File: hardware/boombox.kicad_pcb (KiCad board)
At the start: 2 copper layers, 13 parts, among them J1 Micro_SD_Card_Det1, J5 AudioJack4, U7 MCP7940MT-I/SN, U9 MCP73811T-420I-OT

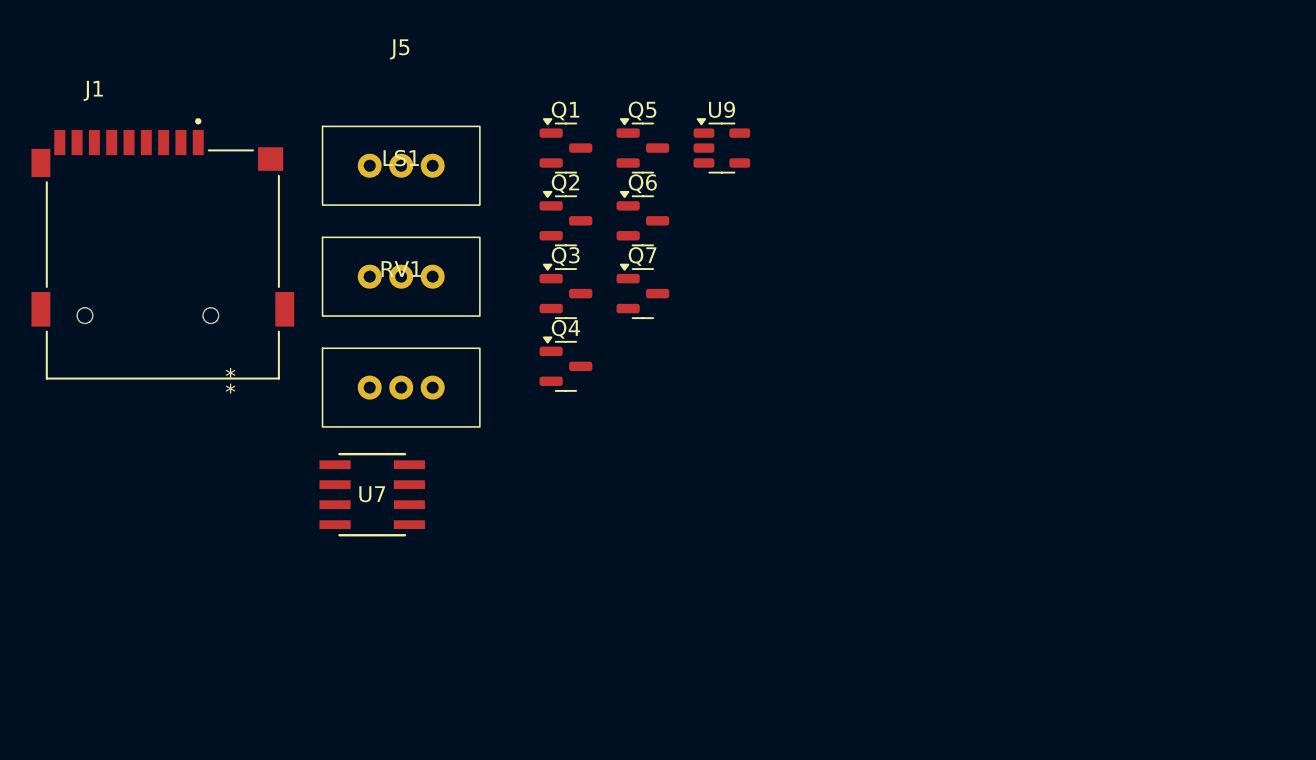
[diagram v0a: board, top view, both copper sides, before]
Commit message: Schematic done
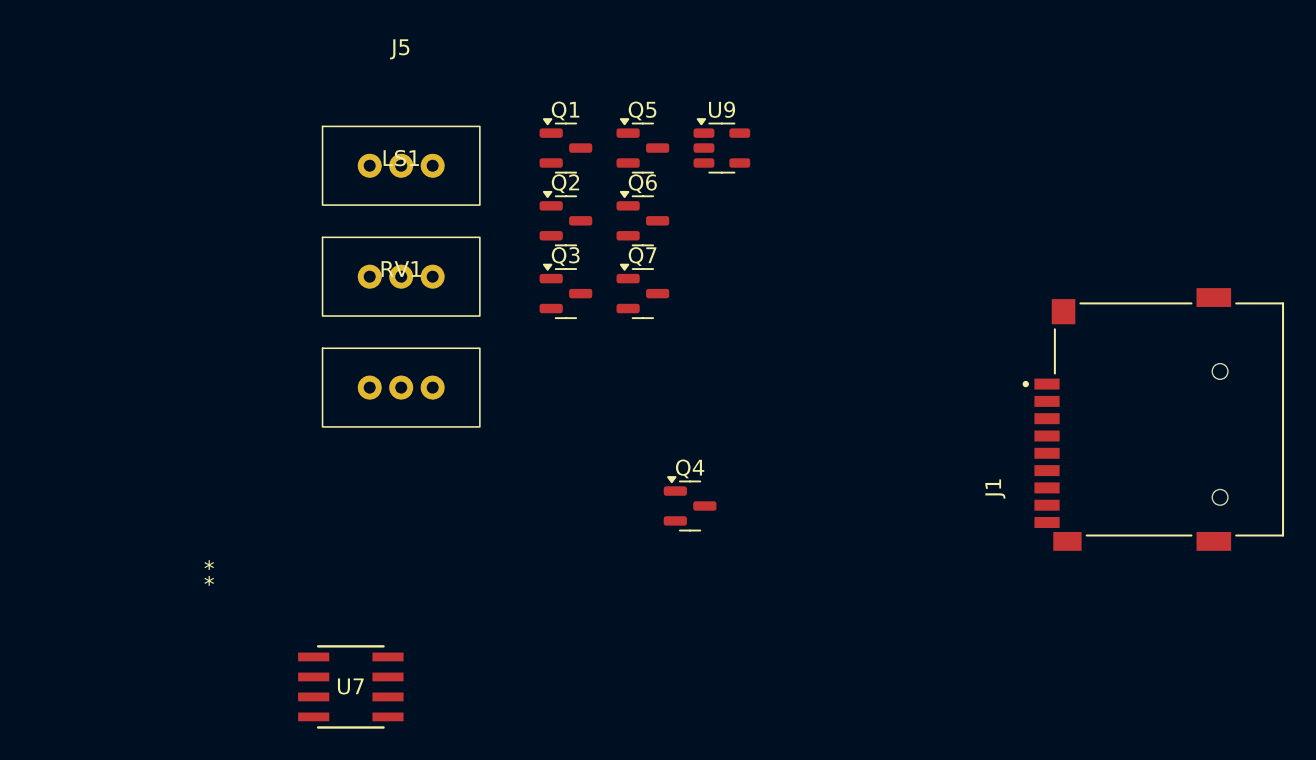
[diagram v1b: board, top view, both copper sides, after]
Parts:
- moved J1 64.7 mm to (192.5, 97.5), turned to 90 degrees
- moved U7 12.3 mm to (140.5, 114.5)
- moved Q4 11.9 mm to (162.1, 103.0)
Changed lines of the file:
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@@
 	(footprint "boombox:SOIC8-N_MC_MCH"
 		(layer "F.Cu")
-		(at 141.8605 102.2813)
+		(at 140.5 114.5)
 		(tags "MCP7940MT-I/SN ")
 		(property "Reference" "U7"
@@
 	(footprint "boombox:CUI_MSD-4-A"
 		(layer "F.Cu")
-		(at 128.5525 87.65)
+		(at 192.5 97.5 90)
 		(property "Reference" "J1"
-			(at -4.325 -11.135 0)
+			(at -4.325 -11.135 90)
 			(layer "F.SilkS")
 			(effects
@@
 		)
 		(property "Value" "Micro_SD_Card_Det1"
-			(at -0.515 -9.635 0)
+			(at -0.515 -9.635 90)
 			(layer "F.Fab")
 			(effects
@@
 		)
 		(property "Footprint" "boombox:CUI_MSD-4-A"
-			(at 0 0 0)
+			(at 0 0 90)
 			(layer "F.Fab")
 			(hide yes)
@@
 		)
 		(property "Datasheet" "${KIPRJMOD}/datasheets/MSD-4-A.pdf"
-			(at 0 0 0)
+			(at 0 0 90)
 			(layer "F.Fab")
 			(hide yes)
@@
 		)
 		(property "Description" "Micro SD Card Socket with one card detection pin"
-			(at 0 0 0)
+			(at 0 0 90)
 			(layer "F.Fab")
 			(hide yes)
@@
 		(attr smd)
 		(fp_line
+			(start 5.73 -7.25)
+			(end 2.92 -7.25)
+			(stroke
+				(width 0.127)
+				(type solid)
+			)
+			(layer "F.SilkS")
+		)
+		(fp_line
+			(start 7.375 -5.63)
+			(end 7.375 1.43)
+			(stroke
+				(width 0.127)
+				(type solid)
+			)
+			(layer "F.SilkS")
+		)
+		(fp_line
 			(start -7.375 -5.23)
 			(end -7.375 1.43)
@@
 		)
 		(fp_line
+			(start 7.375 4.27)
+			(end 7.375 7.25)
+			(stroke
+				(width 0.127)
+				(type solid)
+			)
+			(layer "F.SilkS")
+		)
+		(fp_line
 			(start -7.375 4.27)
 			(end -7.375 7.25)
@@
 		(fp_line
 			(start -7.375 7.25)
-			(end 7.375 7.25)
-			(stroke
-				(width 0.127)
-				(type solid)
-			)
-			(layer "F.SilkS")
-		)
-		(fp_line
-			(start 5.73 -7.25)
-			(end 2.92 -7.25)
-			(stroke
-				(width 0.127)
-				(type solid)
-			)
-			(layer "F.SilkS")
-		)
-		(fp_line
-			(start 7.375 -5.63)
-			(end 7.375 1.43)
-			(stroke
-				(width 0.127)
-				(type solid)
-			)
-			(layer "F.SilkS")
-		)
-		(fp_line
-			(start 7.375 4.27)
 			(end 7.375 7.25)
 			(stroke
@@
 		)
 		(fp_line
+			(start 8.6 -8.8)
+			(end 8.6 13.1)
+			(stroke
+				(width 0.05)
+				(type solid)
+			)
+			(layer "F.CrtYd")
+		)
+		(fp_line
 			(start -8.6 -8.8)
 			(end 8.6 -8.8)
@@
 		)
 		(fp_line
+			(start 8.6 13.1)
+			(end -8.6 13.1)
+			(stroke
+				(width 0.05)
+				(type solid)
+			)
+			(layer "F.CrtYd")
+		)
+		(fp_line
 			(start -8.6 13.1)
 			(end -8.6 -8.8)
@@
 		)
 		(fp_line
-			(start 8.6 -8.8)
-			(end 8.6 13.1)
-			(stroke
-				(width 0.05)
-				(type solid)
-			)
-			(layer "F.CrtYd")
-		)
-		(fp_line
-			(start 8.6 13.1)
-			(end -8.6 13.1)
-			(stroke
-				(width 0.05)
-				(type solid)
-			)
-			(layer "F.CrtYd")
+			(start 7.375 -7.25)
+			(end -7.375 -7.25)
+			(stroke
+				(width 0.127)
+				(type solid)
+			)
+			(layer "F.Fab")
 		)
 		(fp_line
@@
 		)
 		(fp_line
+			(start 7.375 7.25)
+			(end 7.375 -7.25)
+			(stroke
+				(width 0.127)
+				(type solid)
+			)
+			(layer "F.Fab")
+		)
+		(fp_line
+			(start 4.55 7.25)
+			(end 7.375 7.25)
+			(stroke
+				(width 0.127)
+				(type solid)
+			)
+			(layer "F.Fab")
+		)
+		(fp_line
+			(start -6.45 7.25)
+			(end 4.55 7.25)
+			(stroke
+				(width 0.127)
+				(type solid)
+			)
+			(layer "F.Fab")
+		)
+		(fp_line
+			(start -6.45 7.25)
+			(end -6.45 12.35)
+			(stroke
+				(width 0.127)
+				(type solid)
+			)
+			(layer "F.Fab")
+		)
+		(fp_line
 			(start -7.375 7.25)
 			(end -6.45 7.25)
@@
 		)
 		(fp_line
-			(start -6.45 7.25)
-			(end -6.45 12.35)
-			(stroke
-				(width 0.127)
-				(type solid)
-			)
-			(layer "F.Fab")
-		)
-		(fp_line
-			(start -6.45 7.25)
-			(end 4.55 7.25)
-			(stroke
-				(width 0.127)
-				(type solid)
-			)
-			(layer "F.Fab")
-		)
-		(fp_line
 			(start -5.95 9.55)
 			(end 4.05 9.55)
@@
 		)
 		(fp_line
+			(start 4.55 12.35)
+			(end 4.55 7.25)
+			(stroke
+				(width 0.127)
+				(type solid)
+			)
+			(layer "F.Fab")
+		)
+		(fp_line
 			(start -5.95 12.85)
 			(end 4.05 12.85)
@@
 			(layer "F.Fab")
 		)
-		(fp_line
-			(start 4.55 7.25)
-			(end 7.375 7.25)
-			(stroke
-				(width 0.127)
-				(type solid)
-			)
-			(layer "F.Fab")
-		)
-		(fp_line
-			(start 4.55 12.35)
-			(end 4.55 7.25)
-			(stroke
-				(width 0.127)
-				(type solid)
-			)
-			(layer "F.Fab")
-		)
-		(fp_line
-			(start 7.375 -7.25)
-			(end -7.375 -7.25)
-			(stroke
-				(width 0.127)
-				(type solid)
-			)
-			(layer "F.Fab")
-		)
-		(fp_line
-			(start 7.375 7.25)
-			(end 7.375 -7.25)
+		(fp_arc
+			(start 4.55 9.05)
+			(mid 4.403553 9.403553)
+			(end 4.05 9.55)
 			(stroke
 				(width 0.127)
@@
 		)
 		(fp_arc
+			(start 4.55 12.35)
+			(mid 4.403553 12.703553)
+			(end 4.05 12.85)
+			(stroke
+				(width 0.127)
+				(type solid)
+			)
+			(layer "F.Fab")
+		)
+		(fp_arc
 			(start -5.95 12.85)
 			(mid -6.303553 12.703553)
@@
 			(layer "F.Fab")
 		)
-		(fp_arc
-			(start 4.55 9.05)
-			(mid 4.403553 9.403553)
-			(end 4.05 9.55)
-			(stroke
-				(width 0.127)
-				(type solid)
-			)
-			(layer "F.Fab")
-		)
-		(fp_arc
-			(start 4.55 12.35)
-			(mid 4.403553 12.703553)
-			(end 4.05 12.85)
-			(stroke
-				(width 0.127)
-				(type solid)
-			)
-			(layer "F.Fab")
-		)
 		(fp_circle
 			(center 2.25 -9.1)
@@
 		)
 		(pad "" np_thru_hole circle
-			(at -4.95 3.25)
+			(at -4.95 3.25 90)
 			(size 1 1)
 			(drill 1)
@@
 		)
 		(pad "" np_thru_hole circle
-			(at 3.05 3.25)
+			(at 3.05 3.25 90)
 			(size 1 1)
 			(drill 1)
@@
 		)
 		(pad "1" smd rect
-			(at 2.25 -7.75)
+			(at 2.25 -7.75 90)
 			(size 0.7 1.6)
 			(layers "F.Cu" "F.Paste" "F.Mask")
@@
 		)
 		(pad "2" smd rect
-			(at 1.15 -7.75)
+			(at 1.15 -7.75 90)
 			(size 0.7 1.6)
 			(layers "F.Cu" "F.Paste" "F.Mask")
@@
 		)
 		(pad "3" smd rect
-			(at 0.05 -7.75)
+			(at 0.05 -7.75 90)
 			(size 0.7 1.6)
 			(layers "F.Cu" "F.Paste" "F.Mask")
@@
 		)
 		(pad "4" smd rect
-			(at -1.05 -7.75)
+			(at -1.05 -7.75 90)
 			(size 0.7 1.6)
 			(layers "F.Cu" "F.Paste" "F.Mask")
@@
 		)
 		(pad "5" smd rect
-			(at -2.15 -7.75)
+			(at -2.15 -7.75 90)
 			(size 0.7 1.6)
 			(layers "F.Cu" "F.Paste" "F.Mask")
@@
 		)
 		(pad "6" smd rect
-			(at -3.25 -7.75)
+			(at -3.25 -7.75 90)
 			(size 0.7 1.6)
 			(layers "F.Cu" "F.Paste" "F.Mask")
@@
 		)
 		(pad "7" smd rect
-			(at -4.35 -7.75)
+			(at -4.35 -7.75 90)
 			(size 0.7 1.6)
 			(layers "F.Cu" "F.Paste" "F.Mask")
@@
 		)
 		(pad "8" smd rect
-			(at -5.45 -7.75)
+			(at -5.45 -7.75 90)
 			(size 0.7 1.6)
 			(layers "F.Cu" "F.Paste" "F.Mask")
@@
 		)
 		(pad "CD" smd rect
-			(at -6.55 -7.75)
+			(at -6.55 -7.75 90)
 			(size 0.7 1.6)
 			(layers "F.Cu" "F.Paste" "F.Mask")
@@
 		)
 		(pad "G1" smd rect
-			(at -7.75 -6.45)
+			(at -7.75 -6.45 90)
 			(size 1.2 1.8)
 			(layers "F.Cu" "F.Paste" "F.Mask")
@@
 		)
 		(pad "G2" smd rect
-			(at 6.85 -6.7)
+			(at 6.85 -6.7 90)
 			(size 1.6 1.5)
 			(layers "F.Cu" "F.Paste" "F.Mask")
@@
 		)
 		(pad "G3" smd rect
-			(at -7.75 2.85)
+			(at -7.75 2.85 90)
 			(size 1.2 2.2)
 			(layers "F.Cu" "F.Paste" "F.Mask")
@@
 		)
 		(pad "G4" smd rect
-			(at 7.75 2.85)
+			(at 7.75 2.85 90)
 			(size 1.2 2.2)
 			(layers "F.Cu" "F.Paste" "F.Mask")
@@
 	(footprint "Package_TO_SOT_SMD:SOT-23"
 		(layer "F.Cu")
-		(at 154.1725 94.125)
+		(at 162.0625 103)
 		(descr "SOT, 3 Pin (https://www.jedec.org/system/files/docs/to-236h.pdf variant AB), generated with kicad-footprint-generator ipc_gullwing_generator.py")
 		(tags "SOT TO_SOT_SMD")

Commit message: Comitting so Nate can see errors
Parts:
- removed J1: Micro_SD_Card_Det1, boombox:CUI_MSD-4-A
- removed J5: AudioJack4, boombox:Degson 3 Pin
- removed LS1: Speaker, boombox:Degson 3 Pin
- removed Q1, Q2, Q3, Q4, Q5, Q6, Q7: ~, Package_TO_SOT_SMD:SOT-23
- removed RV1: R_Potentiometer_US, boombox:Degson 3 Pin
- removed U7: MCP7940MT-I/SN, boombox:SOIC8-N_MC_MCH
- removed U9: MCP73811T-420I-OT, Package_TO_SOT_SMD:SOT-23-5
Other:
- board outline added: 85 x 70 mm

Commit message: Routing
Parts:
- added C1: 6pF, Capacitor_SMD:C_0402_1005Metric_Pad0.74x0.62mm_HandSolder, F.Cu at (129.4, 89.5)
- added C10: 0.1uF, Capacitor_SMD:C_0402_1005Metric_Pad0.74x0.62mm_HandSolder, F.Cu at (85.5, 121.7)
- added C11: 0.1uF, Capacitor_SMD:C_0402_1005Metric_Pad0.74x0.62mm_HandSolder, F.Cu at (85.5, 123.7)
- added C12: 0.1uF, Capacitor_SMD:C_0402_1005Metric_Pad0.74x0.62mm_HandSolder, F.Cu at (85.5, 125.7)
- added C13: 0.1uF, Capacitor_SMD:C_0402_1005Metric_Pad0.74x0.62mm_HandSolder, F.Cu at (88.7, 117.8)
- added C14: 0.1uF, Capacitor_SMD:C_0402_1005Metric_Pad0.74x0.62mm_HandSolder, F.Cu at (88.7, 119.8)
- added C15: 0.1uF, Capacitor_SMD:C_0402_1005Metric_Pad0.74x0.62mm_HandSolder, F.Cu at (88.7, 121.7)
- added C16: 0.1uF, Capacitor_SMD:C_0402_1005Metric_Pad0.74x0.62mm_HandSolder, F.Cu at (88.7, 123.7)
- added C17: 0.1uF, Capacitor_SMD:C_0402_1005Metric_Pad0.74x0.62mm_HandSolder, F.Cu at (73.1, 120.8)
- added C18: 0.1uF, Capacitor_SMD:C_0402_1005Metric_Pad0.74x0.62mm_HandSolder, F.Cu at (132.6, 165.5)
- added C19: 0.1uF, Capacitor_SMD:C_0402_1005Metric_Pad0.74x0.62mm_HandSolder, F.Cu at (132.6, 167.5)
- added C2: 1nF, Capacitor_SMD:C_0402_1005Metric_Pad0.74x0.62mm_HandSolder, F.Cu at (119.2, 87.2)
- added C20: 0.1uF, Capacitor_SMD:C_0402_1005Metric_Pad0.74x0.62mm_HandSolder, F.Cu at (132.6, 169.4)
- added C21: 10uF, Capacitor_SMD:C_0603_1608Metric_Pad1.08x0.95mm_HandSolder, F.Cu at (193.2, 131.3)
- added C22: 10uF, Capacitor_SMD:C_0603_1608Metric_Pad1.08x0.95mm_HandSolder, F.Cu at (133.1, 171.7)
- added C23: 10uF, Capacitor_SMD:C_0603_1608Metric_Pad1.08x0.95mm_HandSolder, F.Cu at (133.1, 174.2)
- added C3: 6pF, Capacitor_SMD:C_0402_1005Metric_Pad0.74x0.62mm_HandSolder, F.Cu at (128.5, 71.7)
- added C4: 6pF, Capacitor_SMD:C_0402_1005Metric_Pad0.74x0.62mm_HandSolder, F.Cu at (126.6, 78.2)
- added C5: 1nF, Capacitor_SMD:C_0402_1005Metric_Pad0.74x0.62mm_HandSolder, F.Cu at (132.8, 60.2)
- added C6: 1nF, Capacitor_SMD:C_0402_1005Metric_Pad0.74x0.62mm_HandSolder, F.Cu at (132.8, 62.1)
- added C7: 1nF, Capacitor_SMD:C_0402_1005Metric_Pad0.74x0.62mm_HandSolder, F.Cu at (132.8, 64.1)
- added C8: 1nF, Capacitor_SMD:C_0402_1005Metric_Pad0.74x0.62mm_HandSolder, F.Cu at (135.8, 61.4)
- added C9: 1nF, Capacitor_SMD:C_0402_1005Metric_Pad0.74x0.62mm_HandSolder, F.Cu at (135.8, 63.4)
- added D1: D_Dual_CommonCathode_AAK_Split, Package_TO_SOT_SMD:SOT-23, B.Cu at (135.8, 127.8)
- added D11: D_Schottky, Diode_SMD:D_SOD-123, F.Cu at (187.8, 130.1)
- added D12: D_Schottky, Diode_SMD:D_SOD-123, F.Cu at (188.4, 82.0)
- added D2: D_Dual_CommonCathode_AAK_Split, Package_TO_SOT_SMD:SOT-23, B.Cu at (135.7, 79.7)
- added D3: D_Dual_CommonCathode_AAK_Split, Package_TO_SOT_SMD:SOT-23, B.Cu at (136.6, 101.8)
- added D6: D_Dual_CommonCathode_AAK_Split, Package_TO_SOT_SMD:SOT-23, F.Cu at (108.0, -71.2)
- added D7: D_Dual_CommonCathode_AAK_Split, Package_TO_SOT_SMD:SOT-23, F.Cu at (108.0, -67.0)
- added D8: D_Dual_CommonCathode_AAK_Split, Package_TO_SOT_SMD:SOT-23, F.Cu at (108.0, -62.6)
- added J1: Micro_SD_Card_Det1, boombox:CUI_MSD-4-A, B.Cu at (113.7, 101.5)
- added J2: AudioJack4, boombox:EBAA02C_Audio, B.Cu at (185.3, 73.1)
- added J3: Battery, boombox:EBAA02C, B.Cu at (195.3, 73.1)
- added J4: USB_C_Receptacle_USB2.0_16P, boombox:CUI_UJ20-C-H-C-4-SMT-TR, F.Cu at (201.1, 126.5)
- added LS1: Speaker, boombox:EBAA02C, B.Cu at (175.3, 73.1)
- added Q1: ~, Package_TO_SOT_SMD:SOT-23, F.Cu at (116.6, 87.8)
- added Q2: ~, Package_TO_SOT_SMD:SOT-23, F.Cu at (112.5, 87.8)
- added Q3: ~, Package_TO_SOT_SMD:SOT-23, F.Cu at (181.9, 83.0)
- added Q4: ~, Package_TO_SOT_SMD:SOT-23, F.Cu at (132.7, 88.0)
- added Q5: ~, Package_TO_SOT_SMD:SOT-23, F.Cu at (95.7, -71.0)
- added Q6: ~, Package_TO_SOT_SMD:SOT-23, F.Cu at (132.7, 91.8)
- added Q7: ~, Package_TO_SOT_SMD:SOT-23, F.Cu at (114.7, 81.6)
- added R1: 3.3M, Resistor_SMD:R_0402_1005Metric_Pad0.72x0.64mm_HandSolder, F.Cu at (129.3, 90.9)
- added R10: 5.1k, Resistor_SMD:R_0402_1005Metric_Pad0.72x0.64mm_HandSolder, F.Cu at (193.7, 127.8)
- added R11: 5.1k, Resistor_SMD:R_0402_1005Metric_Pad0.72x0.64mm_HandSolder, F.Cu at (198.6, 119.5)
- added R12: 100k, Resistor_SMD:R_0402_1005Metric_Pad0.72x0.64mm_HandSolder, F.Cu at (126.0, 167.4)
- added R13: 0, Resistor_SMD:R_0402_1005Metric_Pad0.72x0.64mm_HandSolder, F.Cu at (126.0, 169.4)
- added R14: 0, Resistor_SMD:R_0402_1005Metric_Pad0.72x0.64mm_HandSolder, F.Cu at (126.0, 171.4)
- added R15: 0, Resistor_SMD:R_0402_1005Metric_Pad0.72x0.64mm_HandSolder, F.Cu at (126.6, 173.2)
- added R16: 1M, Resistor_SMD:R_0402_1005Metric_Pad0.72x0.64mm_HandSolder, F.Cu at (112.4, 172.9)
- added R2: 3.3M, Resistor_SMD:R_0402_1005Metric_Pad0.72x0.64mm_HandSolder, F.Cu at (129.3, 92.8)
- added R3: 1M, Resistor_SMD:R_0402_1005Metric_Pad0.72x0.64mm_HandSolder, F.Cu at (114.0, 85.4)
- added R4: 1M, Resistor_SMD:R_0402_1005Metric_Pad0.72x0.64mm_HandSolder, F.Cu at (109.5, 87.4)
- added R5: 100k, Resistor_SMD:R_0402_1005Metric_Pad0.72x0.64mm_HandSolder, F.Cu at (126.0, 165.4)
- added R6: 10k, Resistor_SMD:R_0402_1005Metric_Pad0.72x0.64mm_HandSolder, F.Cu at (137.4, 78.8)
- added R7: 10k, Resistor_SMD:R_0402_1005Metric_Pad0.72x0.64mm_HandSolder, F.Cu at (137.4, 77.5)
- added R8: 10k, Resistor_SMD:R_0402_1005Metric_Pad0.72x0.64mm_HandSolder, F.Cu at (194.3, 91.3)
- added R9: 10k, Resistor_SMD:R_0402_1005Metric_Pad0.72x0.64mm_HandSolder, F.Cu at (194.3, 94.0)
- added RV1: 500k, boombox:Degson 3 Pin, B.Cu at (174.2, 130.6)
- added SW1: SW_SPST, TestPoint:TestPoint_Pad_2.0x2.0mm, F.Cu at (72.8, -54.4)
- added SW2: SW_SPST, boombox:PTS645S_SMTR92_CNK, F.Cu at (96.7, -79.0)
- added SW3: SW_SPST, boombox:PTS645S_SMTR92_CNK, F.Cu at (107.5, -79.2)
- added SW4: SW_SPST, boombox:PTS645S_SMTR92_CNK, F.Cu at (128.5, -79.2)
- added SW5: SW_SPST, boombox:PTS645S_SMTR92_CNK, F.Cu at (118.0, -79.2)
- added U1: Pico, boombox:RPi_Pico_SMD_TH, F.Cu at (167.2, 102.3)
- added U10: MAX98365A, boombox:MAX98365, F.Cu at (164.0, 144.6)
- added U2: TMAG5231, Package_TO_SOT_SMD:SOT-23, B.Cu at (136.4, 98.0)
- added U3: TMAG5231, Package_TO_SOT_SMD:SOT-23, B.Cu at (151.4, 77.8)
- added U4: TMAG5231, Package_TO_SOT_SMD:SOT-23, B.Cu at (121.4, 77.8)
- added U5: TMAG5231, Package_TO_SOT_SMD:SOT-23, B.Cu at (121.4, 127.8)
- added U6: TMAG5231, Package_TO_SOT_SMD:SOT-23, B.Cu at (151.4, 127.8)
- added U7: MCP7940MT-I/SN, boombox:SOIC8-N_MC_MCH, F.Cu at (131.5, 76.9)
- added U8: MAX98365A, boombox:MAX98365, F.Cu at (115.0, 172.9)
- added U9: MCP73811T-420I-OT, Package_TO_SOT_SMD:SOT-23-5, F.Cu at (198.5, 83.0)
- added Y1: Crystal, boombox:XTAL_ECS-.327-6-13X, F.Cu at (124.7, 73.2)
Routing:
- net SLP_PWR: track 0.00 -> 204.5 mm, vias 0 -> 10
- net Net-(D1A-K): track 0.00 -> 73.1 mm, vias 0 -> 3
- net /Power/POWER IN: track 0.00 -> 70.3 mm, vias 0 -> 4
- net /Power/~{POWER_OFF}: track 0.00 -> 67.2 mm
- net Net-(J1-VDD): track 0.00 -> 63.3 mm, vias 0 -> 2
- net Net-(U1-GPIO5): track 0.00 -> 62.3 mm
- net Net-(J1-DET): track 0.00 -> 49.7 mm
- net GND: track 0.00 -> 44.0 mm, vias 0 -> 24
- net Net-(J1-CMD): track 0.00 -> 36.9 mm
- net /USB_DP: track 0.00 -> 35.3 mm
- net /Power/CLOCK_ALARM: track 0.00 -> 35.2 mm, vias 0 -> 2
- net /USB_DN: track 0.00 -> 34.9 mm
- net Net-(J1-CLK): track 0.00 -> 32.3 mm
- net Net-(J1-DAT3/CD): track 0.00 -> 31.0 mm, vias 0 -> 1
- net Net-(J1-DAT0): track 0.00 -> 23.8 mm
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- added copper zone on B.Cu, net GND
- added copper zone on F.Cu, net GND
- added copper zone on In1.Cu, net GND
- added copper zone on In2.Cu, net GND
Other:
- board size 85 x 70 mm -> 95 x 70 mm
- copper layers 2 -> 4

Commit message: .
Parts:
- removed R12, R5: 100k, Resistor_SMD:R_0402_1005Metric_Pad0.72x0.64mm_HandSolder
- C12, C13, C14, C15, C16, R13, R14, R15, R16: moved to B.Cu
- J2: renamed from LS1; value Speaker -> AudioJack4; footprint boombox:EBAA02C -> boombox:EBAA02C_Audio
- LS1: renamed from J2; value AudioJack4 -> Speaker; footprint boombox:EBAA02C_Audio -> boombox:EBAA02C
- moved D6 117.1 mm to (149.1, 38.5)
- moved D7 117.1 mm to (149.1, 42.7)
- moved D8 117.1 mm to (149.1, 47.0)
- moved Q5 117.1 mm to (136.8, 38.6)
- moved SW2 117.1 mm to (137.8, 30.6)
- moved SW3 117.1 mm to (148.5, 30.5)
- moved SW4 117.1 mm to (169.5, 30.5)
- moved SW5 117.1 mm to (159.0, 30.5)
- moved U8 110.1 mm to (177.6, 82.3)
- moved R16 107.9 mm to (168.2, 80.5), turned to 0 degrees
- moved C22 101.2 mm to (185.5, 85.1), turned to -90 degrees
- moved C23 100.4 mm to (174.3, 82.7), turned to 180 degrees
- moved C18 95.5 mm to (184.0, 85.0), turned to -90 degrees
- moved SW1 95.4 mm to (100.3, 37.0)
- moved C19 93.5 mm to (174.6, 84.0), turned to 180 degrees
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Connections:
- SW2 pad 2: unconnected-(SW2-B-Pad2)_1 -> SLP_PWR
- SW3 pad 2: unconnected-(SW3-B-Pad2)_1 -> SLP_PWR
- SW4 pad 2: unconnected-(SW4-B-Pad2) -> SLP_PWR
- SW5 pad 2: unconnected-(SW5-B-Pad2) -> SLP_PWR
- U10 pad B3: Net-(U10-GAIN_SLOT) -> VCC
- U8 pad B3: Net-(U8-GAIN_SLOT) -> VCC
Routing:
- net VCC: track 3.85 -> 246.4 mm, vias 0 -> 7
- net /Power/MAG_SENSOR3: track 12.5 -> 119.6 mm
- net /Power/MAG_SENSOR4: track 15.6 -> 105.8 mm
- net Net-(U1-GPIO5): track 62.3 -> 2.98 mm
- net Net-(U10-DAI0): track 0.00 -> 51.8 mm, vias 0 -> 4
- net Net-(U10-DAI1): track 0.00 -> 49.9 mm, vias 0 -> 5
- net Net-(U10-DAI2): track 0.00 -> 46.9 mm, vias 0 -> 5
- net /Audio/~{HEADPHONE_DETECT}: track 2.00 -> 44.5 mm, vias 0 -> 2
- net /Power/MAG_SENSOR0: track 2.02 -> 40.6 mm, vias 0 -> 2
- net /Audio/HEADPHONE_EN: track 0.00 -> 35.7 mm, vias 0 -> 2
- net SLP_PWR: track 204.5 -> 239.5 mm, vias 10 -> 12
- net /Power/CLOCK_ALARM: track 35.2 -> 60.5 mm
- net /Audio/VOL: track 0.00 -> 19.5 mm
- net /Audio/SPEAKER_EN: track 0.00 -> 18.8 mm
- net GND: track 44.0 -> 62.0 mm, vias 24 -> 31
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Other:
- board size 95 x 70 mm -> 97.7 x 88.3 mm
